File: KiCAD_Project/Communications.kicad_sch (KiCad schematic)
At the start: 19 parts, among them J10 1-0000190, J9 1-0000050, U4 1-0000446, U5 1-0000785

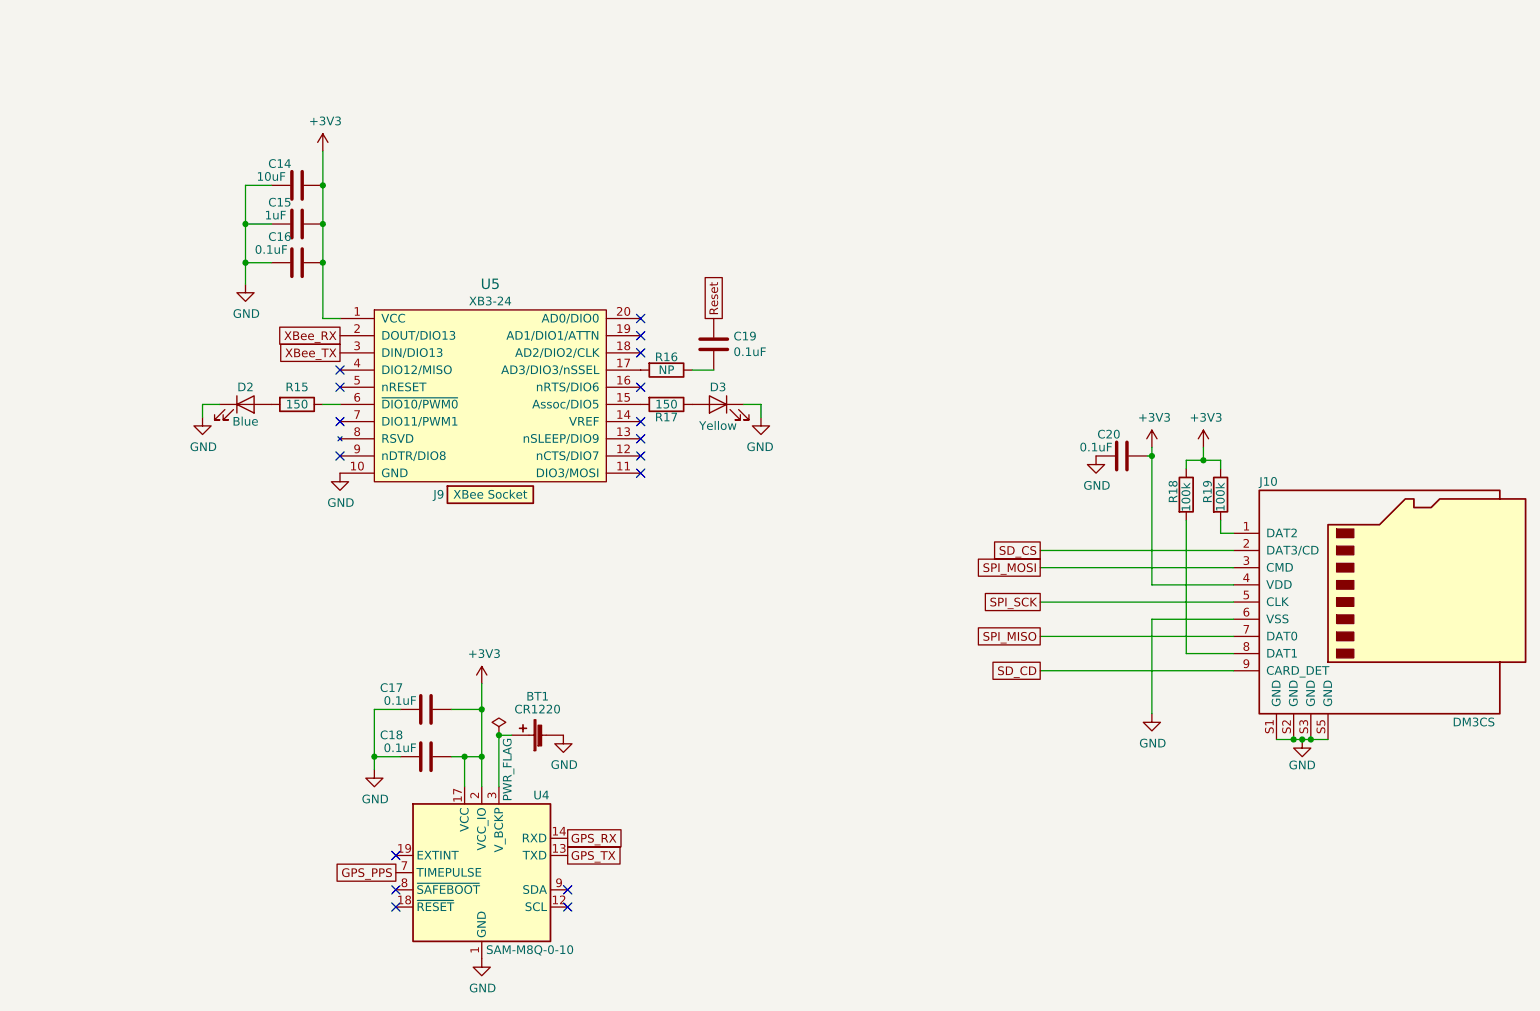
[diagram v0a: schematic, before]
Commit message: Rev 2.0 Changes: Fixed the following issues, - Issue #7 (Added RP Protection) - Issue #6 (Removed old encoder and sense connections) - Issue #5 (Solidified Serial connections by removing jumpers) - Issue #4 (Swapped GPS TX and RX) - Issue #3 (Removed old LED, add SMPL RGB LED) - Issue #2 (Labled ISCP Header) - Issue #1 (Changed DEBUG header to new SMPL DEBUG Connector) Other additions/changes: - Marked all XBEE Components as no pop - Updated board and rev numbers
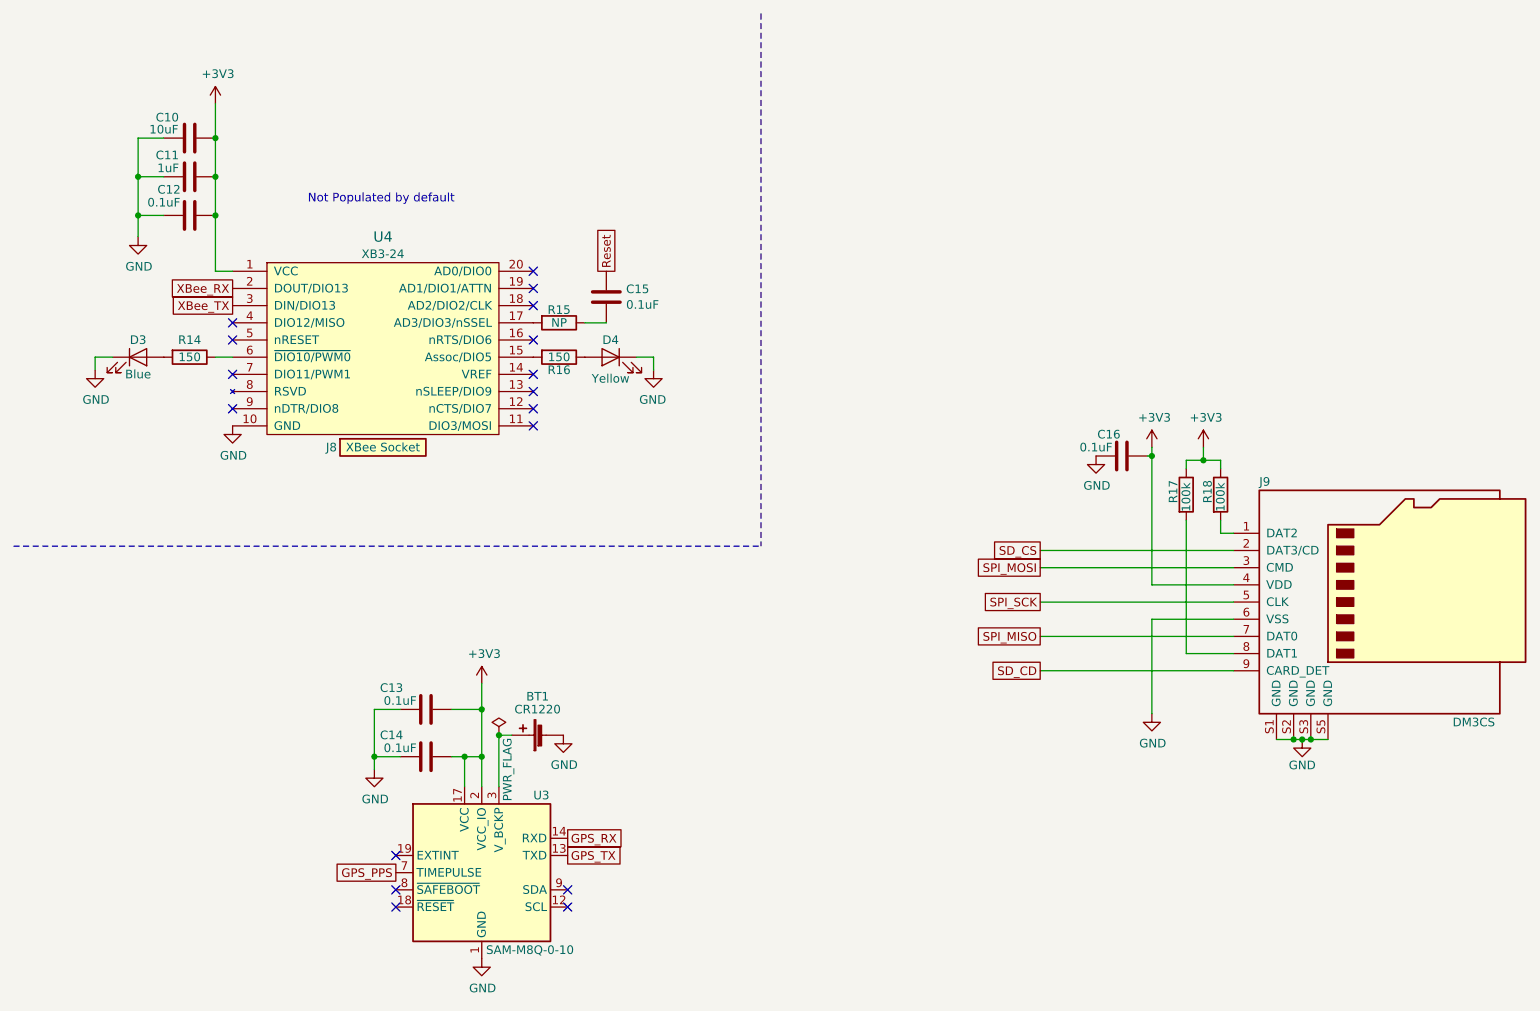
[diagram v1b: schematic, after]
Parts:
- C10: renamed from C14; Populated 1 -> 0
- C11: renamed from C15; Populated 1 -> 0
- C12: renamed from C16; Populated 1 -> 0
- D3: renamed from D2; Populated 1 -> 0
- D4: renamed from D3; Populated 1 -> 0
- J8: renamed from J9; Populated 1 -> 0
- R14: renamed from R15; Populated 1 -> 0
- R16: renamed from R17; Populated 1 -> 0
- U4: renamed from U5; Populated 1 -> 0
- renumbered C17 to C13, C18 to C14, C19 to C15, C20 to C16, J10 to J9, R16 to R15, R18 to R17, R19 to R18, U4 to U3
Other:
- note added: "Not Populated by default"
- moved on the sheet: C10, C11, C12, C15, D3, D4, J8, R14, R15, R16, U4

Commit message: Make Rev 2.0 production files
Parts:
- renumbered U4 to U3, U3 to U4
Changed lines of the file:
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@@
 			"AEcU0AYAAAAAwhgAAAAAAABkaOAEAAAAAEIU0AYAAAAAwxgAAAAAAAC2YuAEAAAAAMEQ0AYAAAAA"
 			"xBgAAAAAAADiGt4EAAAAAKWozgYAAAAAxRgAAAAAAAAm0twEAAAAALc7zgYAAAAAxhgAAAAAAABr"
-			"idsEAAAAAA=="
+			"idsEAAAAAAAAAAAAAAAAAAAAAAAAAAAAAAAAAAAAAAAAAAAAAAAAAAAAAAAAAAAAAAAAAAAAAAAA"
+			"AAAAAAAAAAAAAAAAAAAAAAAAAAAAAAAAAAAAAAAAAAAAAAAAAAAAAAAAAAAAAAAAAAAAAAAAAAAA"
+			"AAAAAAAAAAAAAAAAAAAAAAAAAAAAAAAAAAAAAAAAAAAAAAAAAAAAAAAAAAAAAAAAAAAAAAAAAAAA"
+			"AAAAAAAAAAAAAAAAAAAAAAAAAAAAAAAAAAAAAAAAAAAAAAAAAAAAAAAAAAAAAAAAAAAAAAAAAAAA"
+			"AAAAAAAAAAAAAAAAAAAAAAAAAAAAAAAAAAAAAAAAAAAAAAAAAAAAAAAAAAAAAAAAAAAAAAAAAAAA"
+			"AAAAAAAAAAAAAAAAAAAAAAAAAAAAAAAAAAAAAAAAAAAAAAAAAAAAAAAAAAAAAAAAAAAAAAAAAAAA"
+			"AAAAAAAAAAAAAAAAAAAAAAAAAAAAAAAAAAAAAAAAAAAAAAAAAAAAAAAAAAAAAAAAAAAAAAAAAAAA"
+			"AAAAAAAAAAAAAAAAAAAAAAAAAAAAAAAAAAAAAAAAAAAAAAAAAAAAAAAAAAAAAAAAAAAAAAAAAAAA"
+			"AAAAAAAAAAAAAAAAAAAAAAAAAAAAAAAAAAAAAAAAAAAAAAAAAAAAAAAAAAAAAAAAAAAAAAAAAAAA"
+			"AAAAAAAAAAAAAAAAAAAAAAAAAAAAAAAAAAAAAAAAAAAAAAAAAAAAAAAAAAAAAAAAAAAAAAAAAAAA"
+			"AAAAAAAAAAAAAAAAAAAAAAAAAAAAAAAAAAAAAAAAAAAAAAAAAAAAAAAAAAAAAAAAAAAAAAAAAAAA"
+			"AAAAAAAAAAAAAAAAAAAAAAAAAAAAAAAAAAAAAAAAAAAAAAAAAAAAAAAAAAAAAAAAAAAAAAAAAAAA"
+			"AAAAAAAAAAAAAAAAAAAAAAAAAAAAAAAAAAAAAAAAAAAAAAAAAAAAAAAAAAAAAAAAAAAAAAAAAAAA"
+			"AAAAAAAAAAAAAAAAAAAAAAAAAAAAAAAAAAAAAAAAAAAAAAAAAAAAAAAAAAAAAAAAAAAAAAAAAAAA"
+			"AAAAAAAAAAAAAAAAAAAAAAAAAAAAAAAAAAAAAAAAAAAAAAAAAAAAAAAAAAAAAAAAAAAAAAAAAAAA"
+			"AAAAAAAAAAAAAAAAAAAAAAAAAAAAAAAAAAAAAAAAAAAAAAAAAAAAAAAAAAAAAAAAAAAAAAAAAAAA"
+			"AAAAAAAAAAAAAAAAAAAAAAAAAAAAAAAAAAAAAAAAAAAAAAAAAAAAAAAAAAAAAAAAAAAAAAAAAAAA"
+			"AAAAAAAAAAAAAAAAAAAAAAAAAAAAAAAAAAAAAAAAAAAAAAAAAAAAAAAAAAAAAAAAAAAAAAAAAAAA"
+			"AAAAAAAAAExDAAAAAAAAgU6CngKBiKBMQwAAAAAAAIKwAoLPAhEAgtcC4ILeAuCC5gLggu4C4ND5"
+			"QwAAAAAAAIFOgaiByBEEgc7gglwC0K1DAAAAAAAAgU6ChRWB+IISEIHOEQSCpxXggq4VEQCCuBUR"
+			"AIK/FeCCxhUYCKcX9nnSAACCYALggmgC4IJwAuCCdwLggoAC4IKIAuCCjwLQ5EMAAAAAAACBToKe"
+			"AoGIoORDAAAAAAAAgrACgs8CEQCC1wLggt4C4ILmAuCC7gLg0HRFAAAAAAAAgU6BqIHIEQGBztAk"
+			"RQAAAAAAAIFOgdyB+G8RJEMARgA1ADQARQA1ADgANAAtAEYARAAxADAALQA0ADAAQwA0AC0AQQAz"
+			"AEQAOAAtAEMAQwAyAEUANQBEAEMAMABFADQARQA0AIJIARj//////////4JVAU8RIAAAAAAA8H1A"
+			"AAAAAACoiUAAAAAAAADwPwAAAAAAAPA/gnwBYIKBAREAgocBEQCCkAERAIKYAeCCoQERAIKpAeCC"
+			"sAERAIK5AREAgsIBGNLmJAB60gAAgtEBEeiC2QHgguEBgucBgv8BIwAAAAAAAAAAgg4CgucBghgC"
+			"TxEgAAAAAAAAAAAAAAAAAAAAAAAAAAAAAAAAAAAAAAAAAACCQgIRAIJKAhEAglMCEQCCXALggmAC"
+			"4IJoAuCCcALggncC4IKAAuCCiALggo8C0F9FAAAAAAAAgU6CngKBiKBfRQAAAAAAAIKwAoLPAhEA"
+			"gtcC4ILeAuCC5gLggu4C4ND0RQAAAAAAAIFOgaiByBECgc7QpEUAAAAAAACBToHcgfiCHESCSAER"
+			"QIKHARIWXYJcAuCCYALggmgC4IJwAuCCdwLggoAC4IKIAuCCjwLQ30UAAAAAAACBToKeAoGIoN9F"
+			"AAAAAAAAgrACgs8CEQCC1wLggt4C4ILmAuCC7gLg0JVGAAAAAAAAgU6BqIHIEQKBztBFRgAAAAAA"
+			"AIFOgdyB+IIcRIJIARQAAAAggmoE0EVGAAAAAAAAgU6Bf4GIoEVGAAAAAAAA+BMAAAAAAAAAglwC"
+			"4IJgAuCCaALggnAC4IJ3AuCCgALggogC4IKPAtCARgAAAAAAAIFOgp4CgYiggEYAAAAAAACCsAKC"
+			"zwIRAILXAuCC3gLgguYC4ILuAuDQP0cAAAAAAACBToGogcgRAoHO0O9GAAAAAAAAgU6B3IH4ghxE"
+			"gkgBFAAAACCCagTQ70YAAAAAAACBToF/gYig70YAAAAAAAD4AAAAAAAAAAD4EwAAAAAAAACCXALg"
+			"gmAC4IJoAuCCcALggncC4IKAAuCCiALggo8C0CpHAAAAAAAAgU6CngKBiKAqRwAAAAAAAIKwAoLP"
+			"AhEAgtcC4A=="
 		)
 	)
@@
 		(on_board yes)
 		(dnp no)
-		(property "Reference" "U4"
+		(property "Reference" "U3"
 			(at 67.31 45.72 0)
 			(effects
@@
 			(project "Orientation_Paddle"
 				(path "/6c14ab86-27f6-4df4-bc2f-a5f06a463ed0/817373c8-62ef-4a18-9a02-3efa5f4e7a1a"
-					(reference "U4")
+					(reference "U3")
 					(unit 1)
 				)
@@
 		(on_board yes)
 		(dnp no)
-		(property "Reference" "U3"
+		(property "Reference" "U4"
 			(at 89.535 128.27 0)
 			(effects
@@
 			(project "Orientation_Paddle"
 				(path "/6c14ab86-27f6-4df4-bc2f-a5f06a463ed0/817373c8-62ef-4a18-9a02-3efa5f4e7a1a"
-					(reference "U3")
+					(reference "U4")
 					(unit 1)
 				)

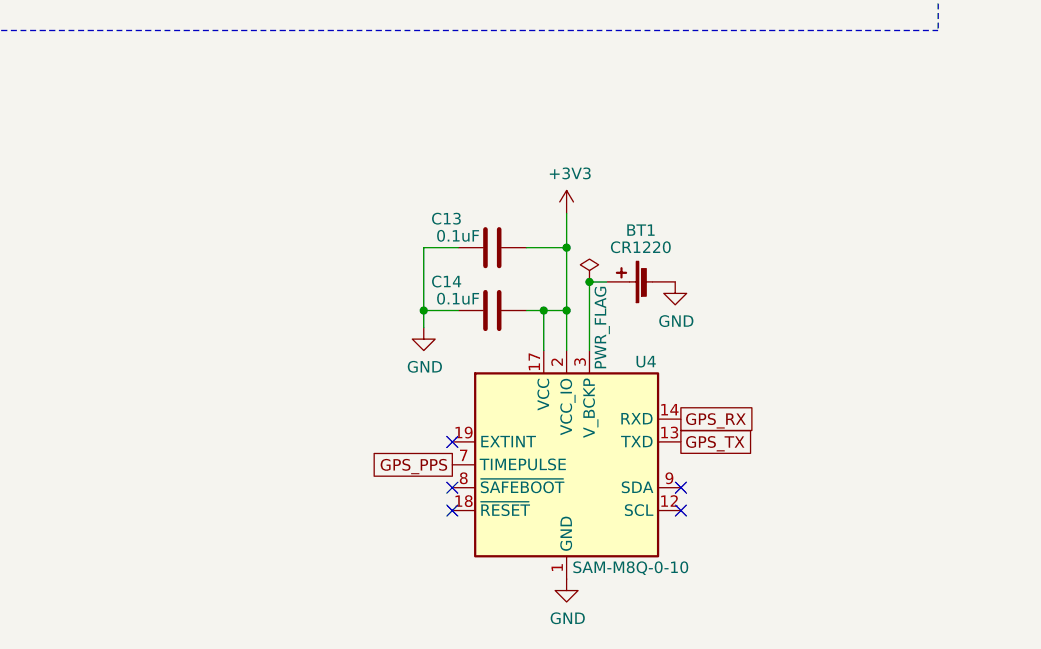
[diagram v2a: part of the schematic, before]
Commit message: Fixed Issues #9, Issue #10 (Rev2.1)
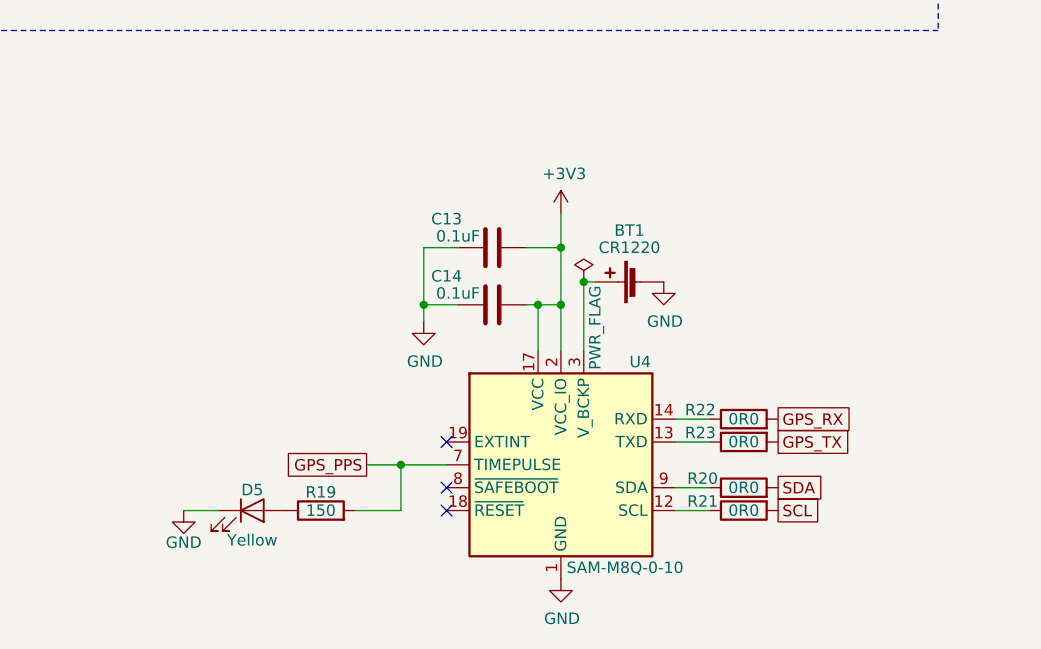
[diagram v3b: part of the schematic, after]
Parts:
- added D5: 1-0000601, leds_0805:1-0000601, symbol leds_0805:1-0000601
- added R19: 1-0000008, resistors_0603:1-0000008, symbol resistors_0603:1-0000008
- added R20, R21, R22, R23: 1-0000006, resistors_0603:1-0000006, symbol resistors_0603:1-0000006
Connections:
- net GND: now also D5.1 (K)
- net GPS_PPS: now also R19.2
- net GPS_RX: now also R22.2; no longer U4.14 (RXD)
- net GPS_TX: now also R23.2; no longer U4.13 (TXD)
- net at U4.12 (SCL): now also R21.1
- net at U4.9 (SDA): now also R20.1
- new net: R22.1, U4.14 (RXD)
- new net: D5.2 (A), R19.1
- new net: R23.1, U4.13 (TXD)
- new net SCL: R21.2
- new net SDA: R20.2
- no-connect marks 17 -> 15
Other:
- moved on the sheet: BT1, C14, U4

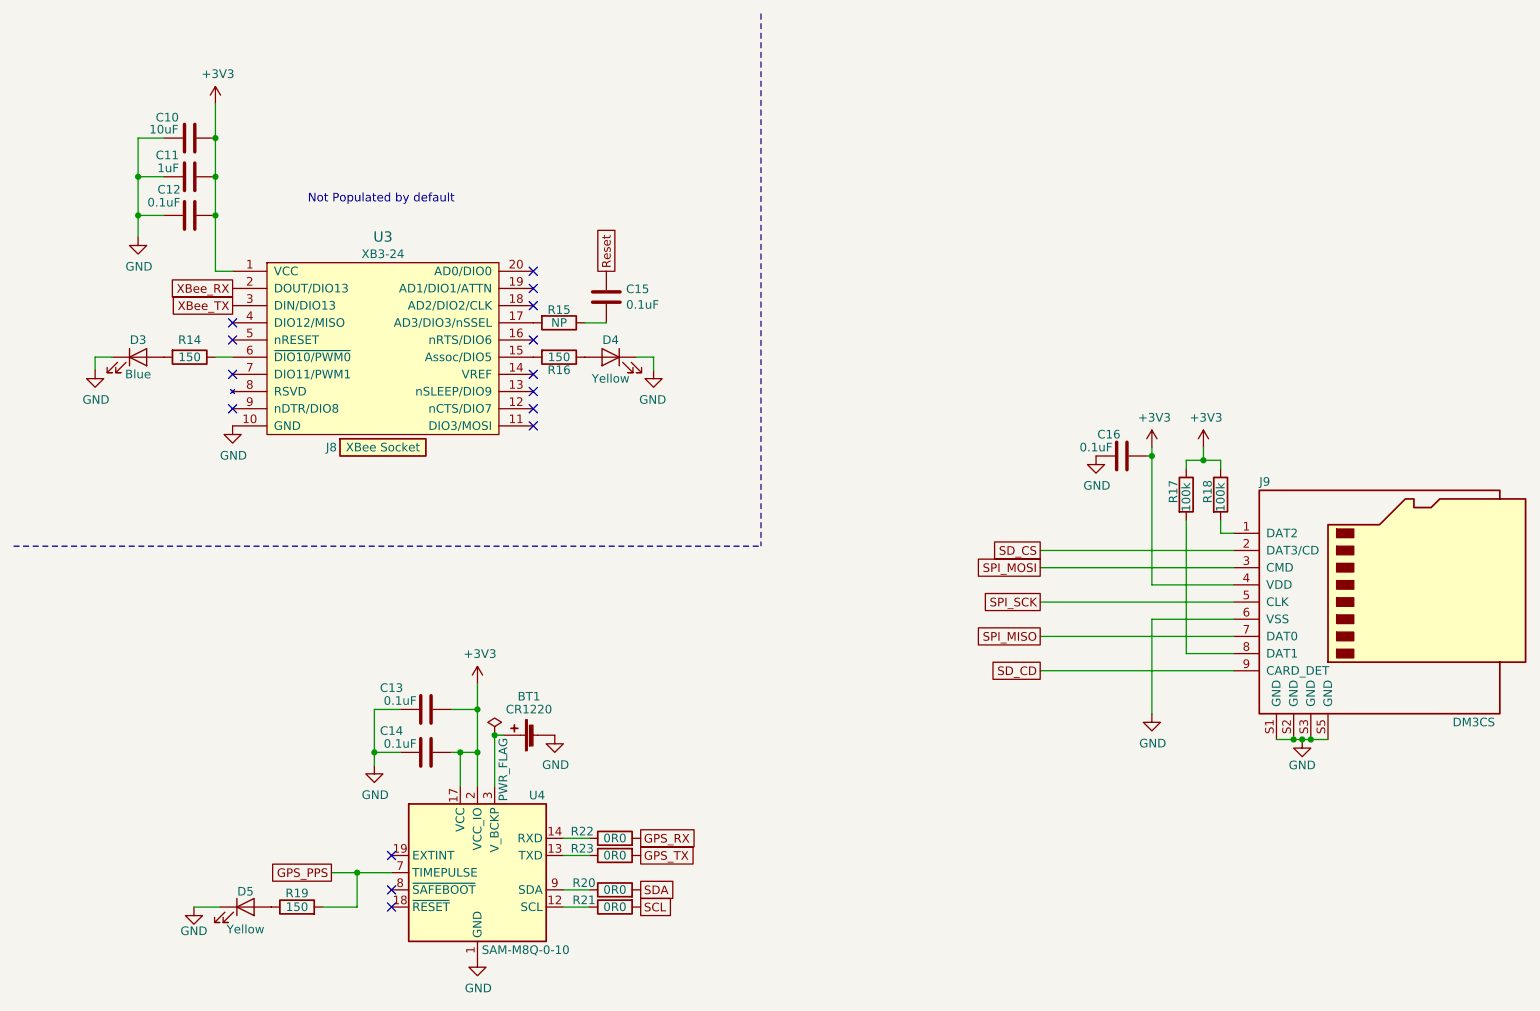
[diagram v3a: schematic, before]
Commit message: Add serial jumpers for GPS and make production files for Rev 2.1
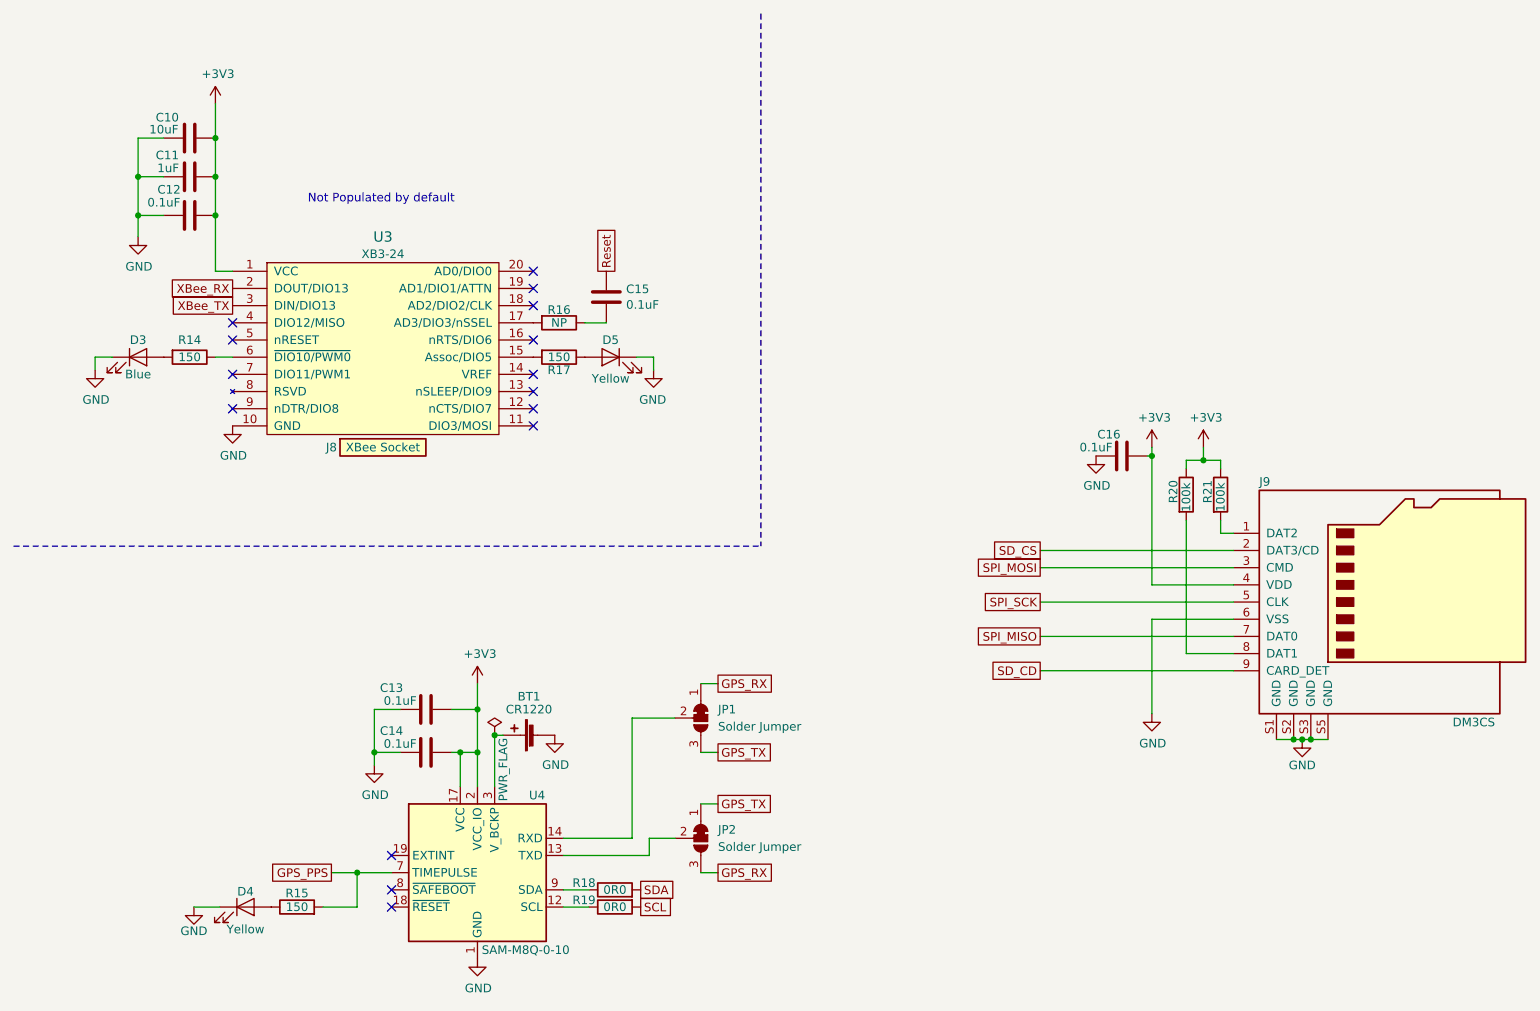
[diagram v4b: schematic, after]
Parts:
- removed R22, R23: 1-0000006, resistors_0603:1-0000006, symbol resistors_0603:1-0000006
- added JP1, JP2: SolderJumper_3_Bridged12, np_connectors:SolderJumper-3_P1.3mm_Bridged12_RoundedPad1.0x1.5mm, symbol np_connectors:SolderJumper_3_Bridged12
- renumbered D5 to D4, D4 to D5, R19 to R15, R15 to R16, R16 to R17, R20 to R18, R21 to R19, R17 to R20, R18 to R21
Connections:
- net GPS_RX: now also JP1.1 (A), JP2.3 (B)
- net GPS_TX: now also JP1.3 (B), JP2.1 (A)
- net at U4.14 (RXD): now also JP1.2 (C)
- net at U4.13 (TXD): now also JP2.2 (C)
